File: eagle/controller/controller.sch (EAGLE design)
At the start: 35 parts, among them IC1 ATMEGA48/88/168-PU, K1 REED, K2 REED, K3 REED, Q1 BC517, Q2 BC517, Q3 BC517, X1 43160-1102, X2 43160-1102, X3 43160-1102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

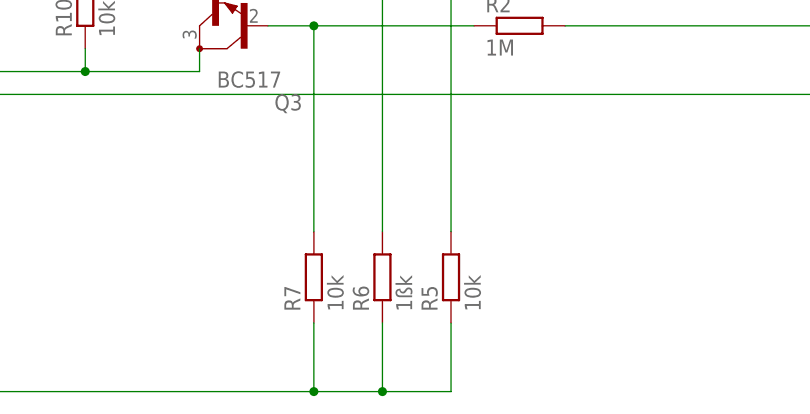
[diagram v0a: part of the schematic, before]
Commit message: Change a designation
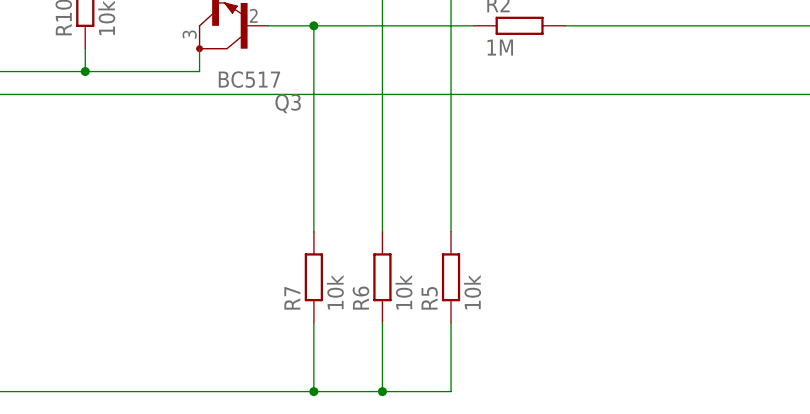
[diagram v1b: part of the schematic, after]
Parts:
- R6: value 1ßk -> 10k
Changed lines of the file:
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@@
 <part name="R4" library="resistor" deviceset="R-EU_" device="0204/7" value="1M"/>
 <part name="R5" library="resistor" deviceset="R-EU_" device="0204/7" value="10k"/>
-<part name="R6" library="resistor" deviceset="R-EU_" device="0204/7" value="1ßk"/>
+<part name="R6" library="resistor" deviceset="R-EU_" device="0204/7" value="10k"/>
 <part name="R7" library="resistor" deviceset="R-EU_" device="0204/7" value="10k"/>
 <part name="R8" library="resistor" deviceset="R-EU_" device="0204/7" value="10k"/>

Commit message: Complete the circuit
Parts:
- added B4: (no value), e-messfuehler:MESSFUEHLER_2
- added F2: (no value), e-sicherungen:SICHERUNG_1-POL
- added POWER230V1: C-GRID-02-15-19, con-molex:C-GRID-02-15-19
- added Q4: BC517, transistor-npn:BC517
- added R12, R13: 1M, resistor:R-EU_0204/7
- added R14, R15: 10k, resistor:R-EU_0204/7
- added X6: 43160-1102, con-molex:43160-1102
- K1, K2: value REED -> (none); device relay:REED -> e-schuetze-relais:HILFSSCHUETZ_13-14; TYPE (none) -> JS 05 MN KT
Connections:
- removed net N$3 (its old number): IC4.O3, K11.-
- new net N$18: IC1.PD3(INT1/OC2B/PCINT19), Q4.C, R14.1
- new net N$31: IC4.O2, K2G$1.A2
- new net N$33: F2.2
- new net N$34: F2.1, POWER230V1-1.S
- new net N$35: K21.4, POWER230V1-2.S
- new net N$5: B4.1
- net GND: now also Q4.E, R15.1
- net N$1: now also K1G$1.A2
- net N$10: now also X6-1.S@2; no longer K22.P, X2-2.S@1
- net N$11: now also Q4.B, R13.1, R15.2; no longer K12.P, X3-2.S@1
- net N$12: now also R12.1
- net N$17: now also R12.2
- net N$4: now also B4.2; no longer IC4.O2, K21.-
- net N$9: now also X2-2.S@1, X3-2.S@1, X6-2.S@1
- net VCC: now also K1G$1.A1, K2G$1.A1, R14.2; no longer K11.+, K12.S, K21.+, K22.S
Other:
- moved on the sheet: F1, K6, R2, R3, R4, R5, R6, R7

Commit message: corrected errors
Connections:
- net N$10: now also X6-1.S@1; no longer X6-1.S@2
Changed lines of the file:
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@@
 <wire x1="353.06" y1="7.62" x2="381" y2="7.62" width="0.1524" layer="91"/>
-</segment>
-<segment>
-<wire x1="350.52" y1="5.08" x2="378.46" y2="5.08" width="0.1524" layer="91"/>
-</segment>
-</net>
-<net name="N$27" class="0">
-<segment>
-<pinref part="B3" gate="G$1" pin="1"/>
-<wire x1="353.06" y1="5.08" x2="396.24" y2="5.08" width="0.1524" layer="91"/>
 </segment>
 </net>
@@
 <pinref part="SV1" gate="G$1" pin="10"/>
 <wire x1="53.34" y1="121.92" x2="53.34" y2="129.54" width="0.1524" layer="91"/>
+<junction x="53.34" y="129.54"/>
 </segment>
 <segment>
@@
 <pinref part="R14" gate="G$1" pin="1"/>
 <wire x1="261.62" y1="-27.94" x2="261.62" y2="-22.86" width="0.1524" layer="91"/>
+<junction x="261.62" y="-27.94"/>
 </segment>
 </net>
 <net name="N$10" class="0">
 <segment>
-<pinref part="X6" gate="-1" pin="S@2"/>
-<wire x1="350.52" y1="-22.86" x2="342.9" y2="-22.86" width="0.1524" layer="91"/>
 <wire x1="342.9" y1="-22.86" x2="342.9" y2="-20.32" width="0.1524" layer="91"/>
 <wire x1="342.9" y1="-20.32" x2="320.04" y2="-20.32" width="0.1524" layer="91"/>
+<pinref part="X6" gate="-1" pin="S@1"/>
+<wire x1="347.98" y1="-22.86" x2="342.9" y2="-22.86" width="0.1524" layer="91"/>
 </segment>
 </net>
@@
 </segment>
 </net>
+<net name="N$27" class="0">
+<segment>
+<pinref part="B3" gate="G$1" pin="1"/>
+<wire x1="396.24" y1="5.08" x2="353.06" y2="5.08" width="0.1524" layer="91"/>
+</segment>
+</net>

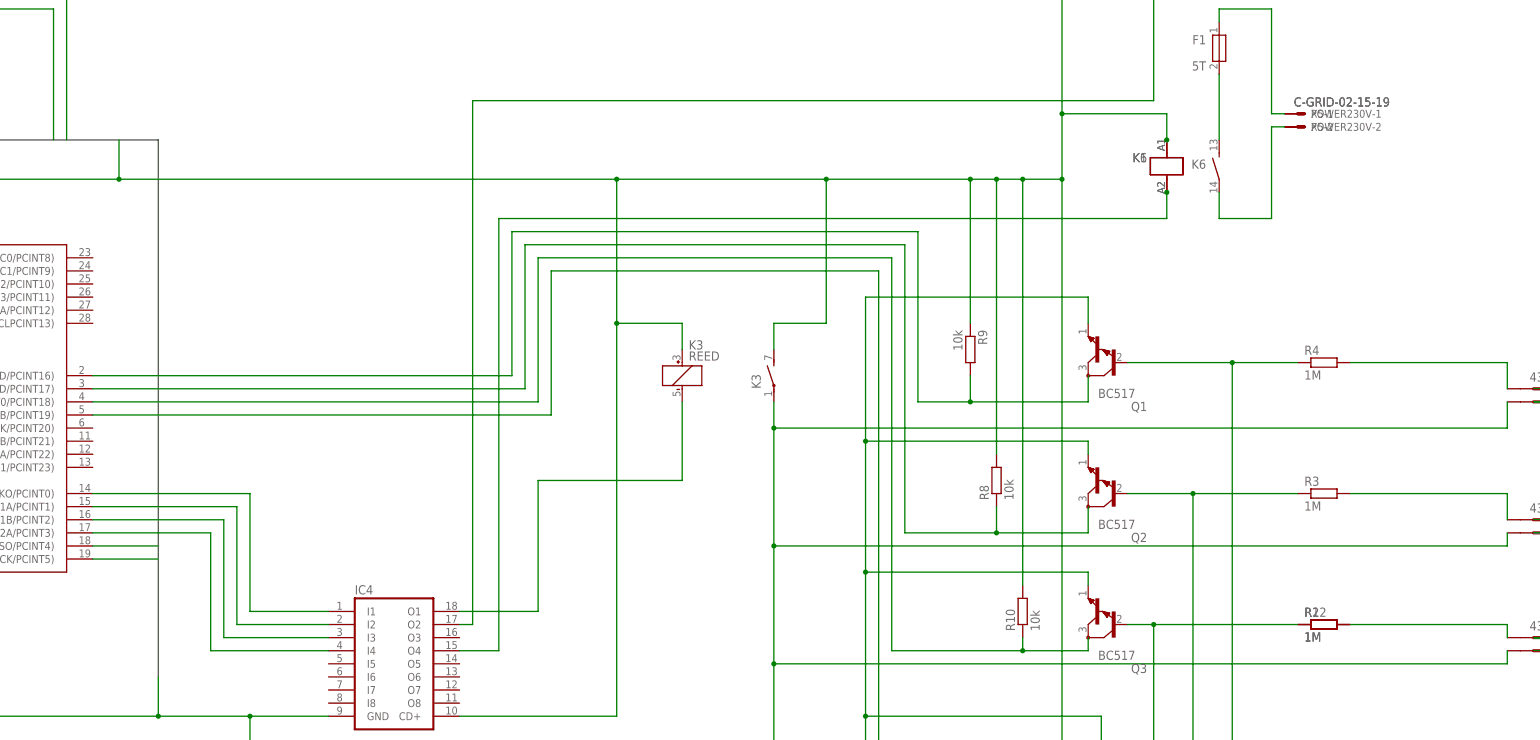
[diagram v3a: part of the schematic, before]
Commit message: components removed
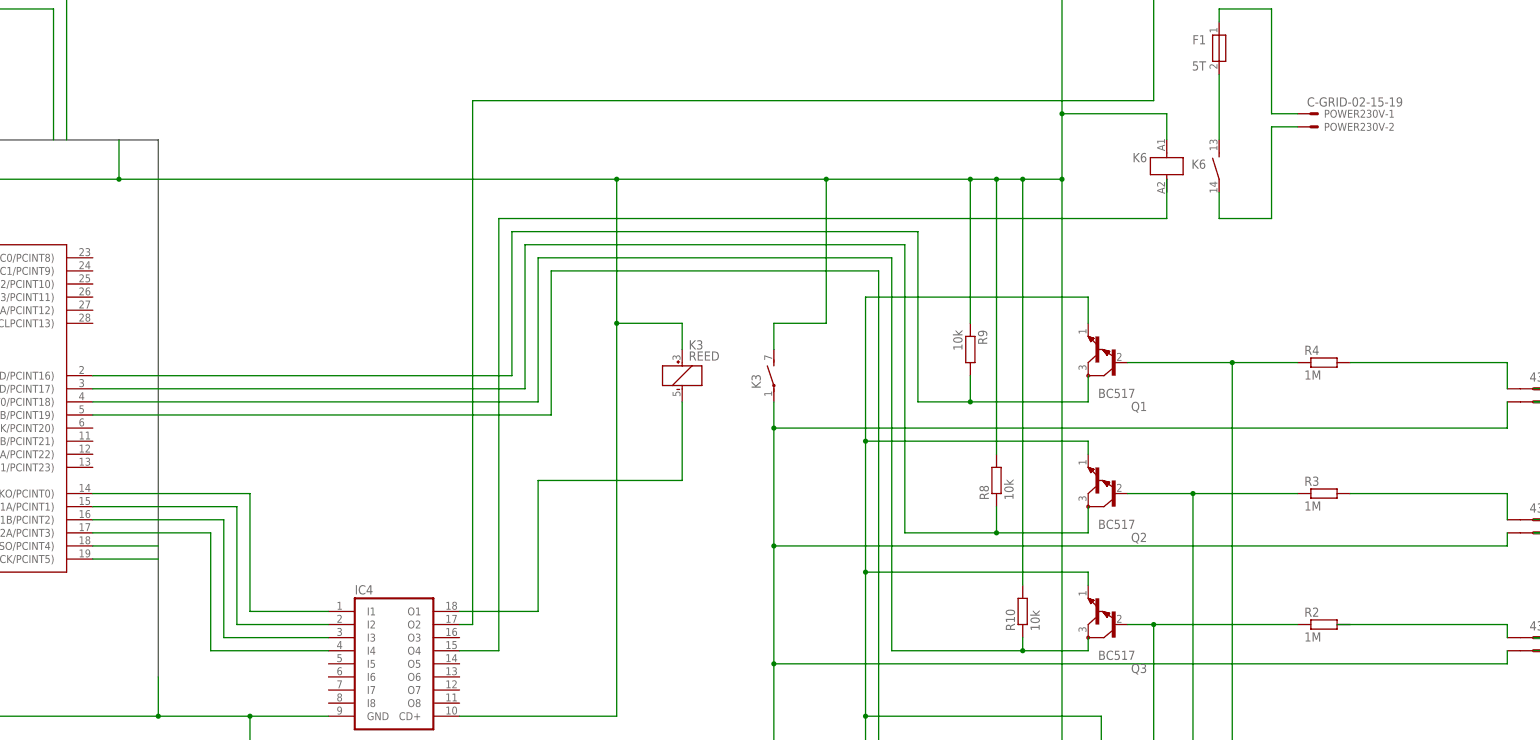
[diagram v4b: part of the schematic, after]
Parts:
- removed K1: (no value), e-schuetze-relais:HILFSSCHUETZ_13-14
- removed R12: 1M, resistor:R-EU_0204/7
- removed X5: C-GRID-02-15-19, con-molex:C-GRID-02-15-19
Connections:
- net N$1: no longer K1G$1.A2, K6G$1.A2
- net N$12: no longer R12.1
- net N$17: no longer R12.2
- net N$30: no longer X5-2.S
- net N$32: no longer X5-1.S
- net VCC: no longer K1G$1.A1
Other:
- moved on the sheet: POWER230V-1, POWER230V-2
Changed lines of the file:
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@@
 </part>
 <part name="X4" library="con-berg" deviceset="PN87520" device=""/>
-<part name="X5" library="con-molex" deviceset="C-GRID-02" device="-15-19"/>
 <part name="POWER230V" library="con-molex" deviceset="C-GRID-02" device="-15-19"/>
 <part name="C2" library="resistor" deviceset="C-EU" device="025-030X050" value="100n"/>
@@
 </part>
 <part name="X6" library="con-molex" deviceset="43160-*02" device="" technology="11"/>
-<part name="R12" library="resistor" deviceset="R-EU_" device="0204/7" value="1M"/>
 <part name="R13" library="resistor" deviceset="R-EU_" device="0204/7" value="1M"/>
 <part name="Q4" library="transistor-npn" deviceset="BC517*" device=""/>
 <part name="R14" library="resistor" deviceset="R-EU_" device="0204/7" value="10k"/>
 <part name="R15" library="resistor" deviceset="R-EU_" device="0204/7" value="10k"/>
-<part name="K1" library="e-schuetze-relais" deviceset="HILFSSCHUETZ_13-14" device="">
-<attribute name="TYPE" value="JS 05 MN KT"/>
-</part>
 <part name="K2" library="e-schuetze-relais" deviceset="HILFSSCHUETZ_13-14" device="">
 <attribute name="TYPE" value="JS 05 MN KT"/>
@@
 <instance part="F1" gate="G$1" x="292.1" y="121.92"/>
 <instance part="X4" gate="G$1" x="-86.36" y="50.8" rot="MR0"/>
-<instance part="X5" gate="-2" x="307.34" y="106.68"/>
-<instance part="X5" gate="-1" x="307.34" y="109.22"/>
-<instance part="POWER230V" gate="-2" x="307.34" y="106.68"/>
-<instance part="POWER230V" gate="-1" x="307.34" y="109.22"/>
+<instance part="POWER230V" gate="-2" x="309.88" y="106.68"/>
+<instance part="POWER230V" gate="-1" x="309.88" y="109.22"/>
 <instance part="C2" gate="G$1" x="-40.64" y="55.88"/>
 <instance part="SV1" gate="G$1" x="45.72" y="127" rot="R180"/>
@@
 <instance part="X6" gate="-1" x="353.06" y="-22.86"/>
 <instance part="X6" gate="-2" x="353.06" y="-25.4"/>
-<instance part="R12" gate="G$1" x="312.42" y="10.16"/>
 <instance part="R13" gate="G$1" x="317.5" y="-20.32"/>
 <instance part="Q4" gate="G$1" x="274.32" y="-20.32" rot="R180"/>
 <instance part="R14" gate="G$1" x="261.62" y="-17.78" rot="R90"/>
 <instance part="R15" gate="G$1" x="302.26" y="-40.64" rot="R90"/>
-<instance part="K1" gate="G$1" x="281.94" y="99.06">
-<attribute name="FUNKTION" x="281.94" y="99.06" size="1.778" layer="96" display="off"/>
-<attribute name="TYPE" x="281.94" y="99.06" size="1.778" layer="96" display="off"/>
-</instance>
 <instance part="K2" gate="G$1" x="279.4" y="154.94"/>
 <instance part="K2" gate="1" x="292.1" y="154.94"/>
@@
 <wire x1="279.4" y1="-35.56" x2="279.4" y2="10.16" width="0.1524" layer="91"/>
 <junction x="279.4" y="10.16"/>
-<pinref part="R12" gate="G$1" pin="1"/>
 </segment>
 </net>
@@
 <wire x1="347.98" y1="10.16" x2="347.98" y2="7.62" width="0.1524" layer="91"/>
 <pinref part="R2" gate="G$1" pin="2"/>
-<pinref part="R12" gate="G$1" pin="2"/>
 <wire x1="347.98" y1="10.16" x2="317.5" y2="10.16" width="0.1524" layer="91"/>
+<wire x1="314.96" y1="10.16" x2="317.5" y2="10.16" width="0.1524" layer="91"/>
 </segment>
 </net>
@@
 <wire x1="144.78" y1="5.08" x2="152.4" y2="5.08" width="0.1524" layer="91"/>
 <wire x1="152.4" y1="5.08" x2="152.4" y2="88.9" width="0.1524" layer="91"/>
-<pinref part="K6" gate="G$1" pin="A2"/>
 <wire x1="152.4" y1="88.9" x2="281.94" y2="88.9" width="0.1524" layer="91"/>
-<wire x1="281.94" y1="88.9" x2="281.94" y2="93.98" width="0.1524" layer="91"/>
-<pinref part="K1" gate="G$1" pin="A2"/>
-<junction x="281.94" y="93.98"/>
+<wire x1="281.94" y1="88.9" x2="281.94" y2="96.52" width="0.1524" layer="91"/>
 </segment>
 </net>
@@
 <wire x1="292.1" y1="88.9" x2="302.26" y2="88.9" width="0.1524" layer="91"/>
 <wire x1="302.26" y1="88.9" x2="302.26" y2="106.68" width="0.1524" layer="91"/>
-<pinref part="X5" gate="-2" pin="S"/>
 <pinref part="POWER230V" gate="-2" pin="S"/>
-<wire x1="302.26" y1="106.68" x2="304.8" y2="106.68" width="0.1524" layer="91"/>
+<wire x1="302.26" y1="106.68" x2="307.34" y2="106.68" width="0.1524" layer="91"/>
 </segment>
 </net>
 <net name="N$32" class="0">
 <segment>
-<pinref part="X5" gate="-1" pin="S"/>
 <pinref part="POWER230V" gate="-1" pin="S"/>
 <pinref part="F1" gate="G$1" pin="1"/>
@@
 <wire x1="292.1" y1="129.54" x2="302.26" y2="129.54" width="0.1524" layer="91"/>
 <wire x1="302.26" y1="129.54" x2="302.26" y2="109.22" width="0.1524" layer="91"/>
-<wire x1="304.8" y1="109.22" x2="302.26" y2="109.22" width="0.1524" layer="91"/>
+<wire x1="307.34" y1="109.22" x2="302.26" y2="109.22" width="0.1524" layer="91"/>
 </segment>
 </net>
@@
 </segment>
 <segment>
-<pinref part="IC1" gate="1" pin="PB3(MOSI/OC2A/PCINT3)"/>
-<wire x1="86.36" y1="27.94" x2="96.52" y2="27.94" width="0.1524" layer="91"/>
-<wire x1="96.52" y1="27.94" x2="96.52" y2="5.08" width="0.1524" layer="91"/>
 <pinref part="IC4" gate="G$1" pin="I4"/>
 <wire x1="96.52" y1="5.08" x2="119.38" y2="5.08" width="0.1524" layer="91"/>
-<wire x1="86.36" y1="27.94" x2="73.66" y2="27.94" width="0.1524" layer="91"/>
+<pinref part="IC1" gate="1" pin="PB3(MOSI/OC2A/PCINT3)"/>
+<wire x1="73.66" y1="27.94" x2="96.52" y2="27.94" width="0.1524" layer="91"/>
+<wire x1="96.52" y1="27.94" x2="96.52" y2="5.08" width="0.1524" layer="91"/>
 </segment>
 </net>
@@
 <pinref part="R14" gate="G$1" pin="2"/>
 <wire x1="261.62" y1="96.52" x2="261.62" y2="-12.7" width="0.1524" layer="91"/>
-<pinref part="K1" gate="G$1" pin="A1"/>
-<junction x="281.94" y="104.14"/>
 <pinref part="K2" gate="G$1" pin="A1"/>
 <wire x1="279.4" y1="160.02" x2="279.4" y2="165.1" width="0.1524" layer="91"/>
